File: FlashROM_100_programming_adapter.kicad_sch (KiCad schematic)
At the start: 2 parts

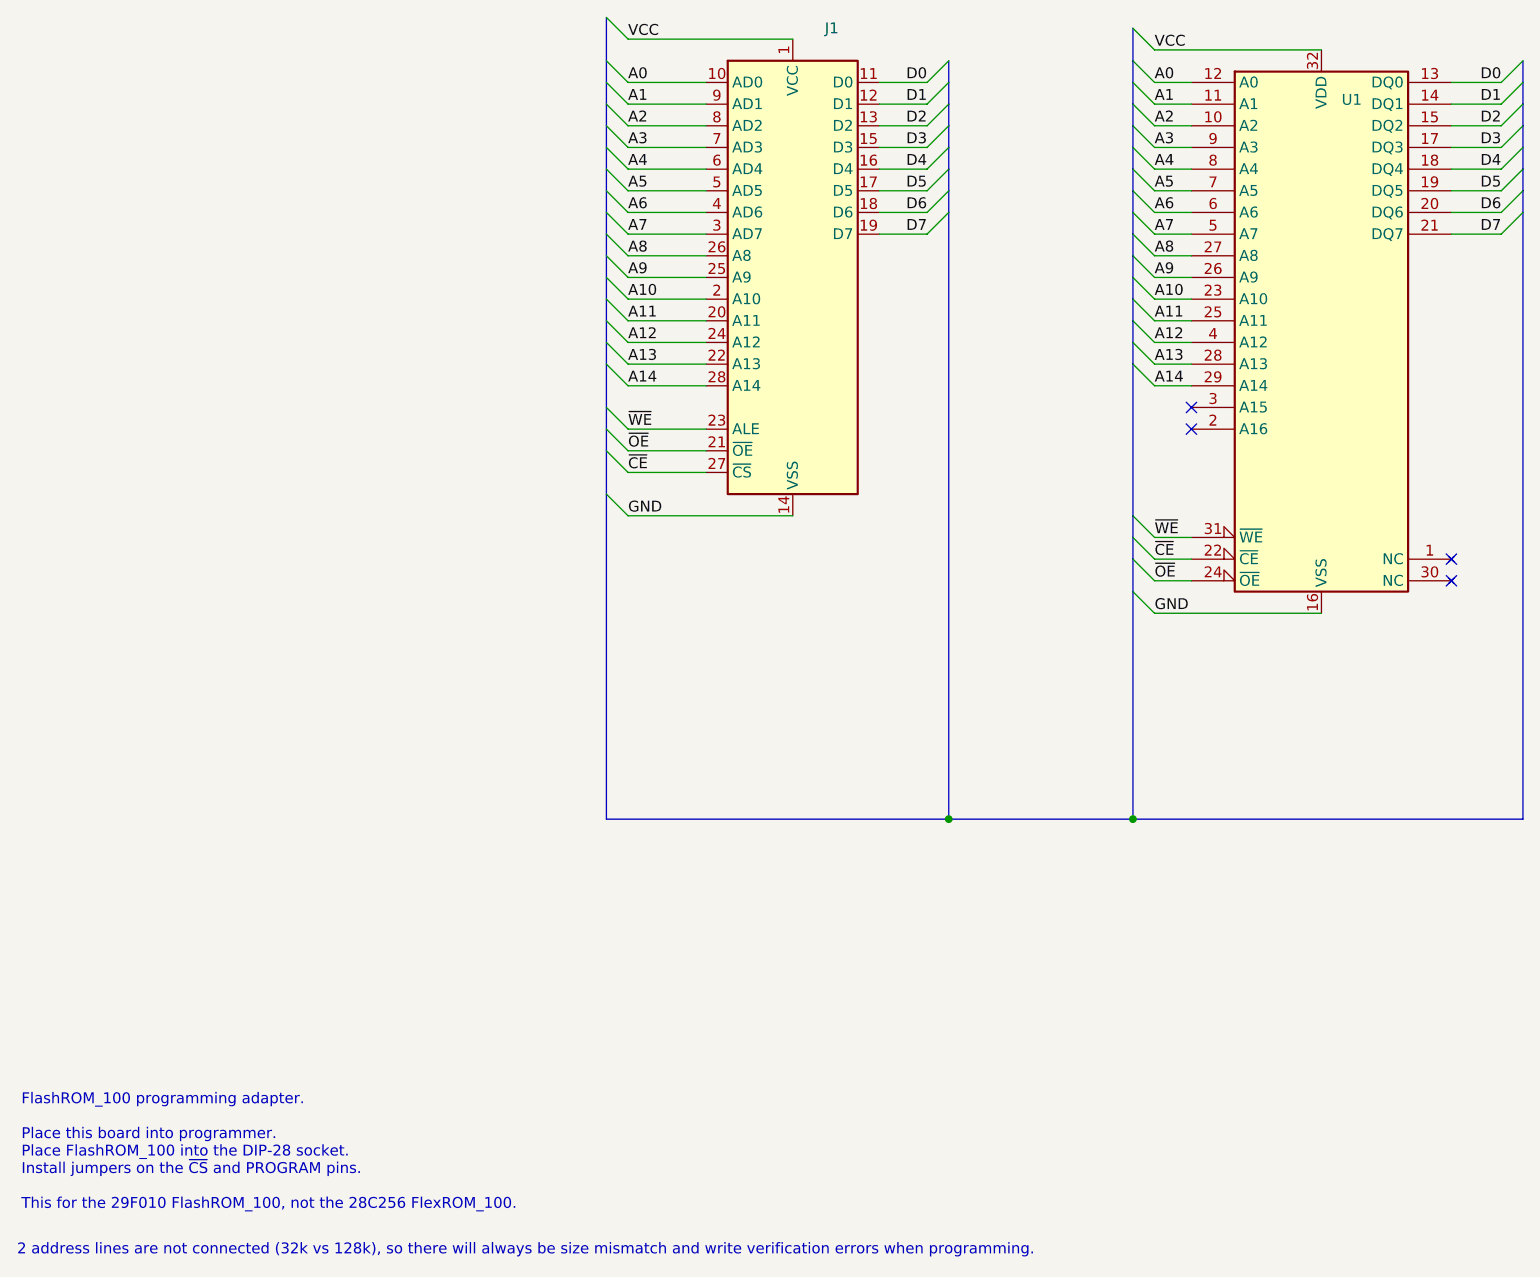
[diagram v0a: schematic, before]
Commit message: Fix wrong pinout on FlashROM_100 TSOPgit add -A!
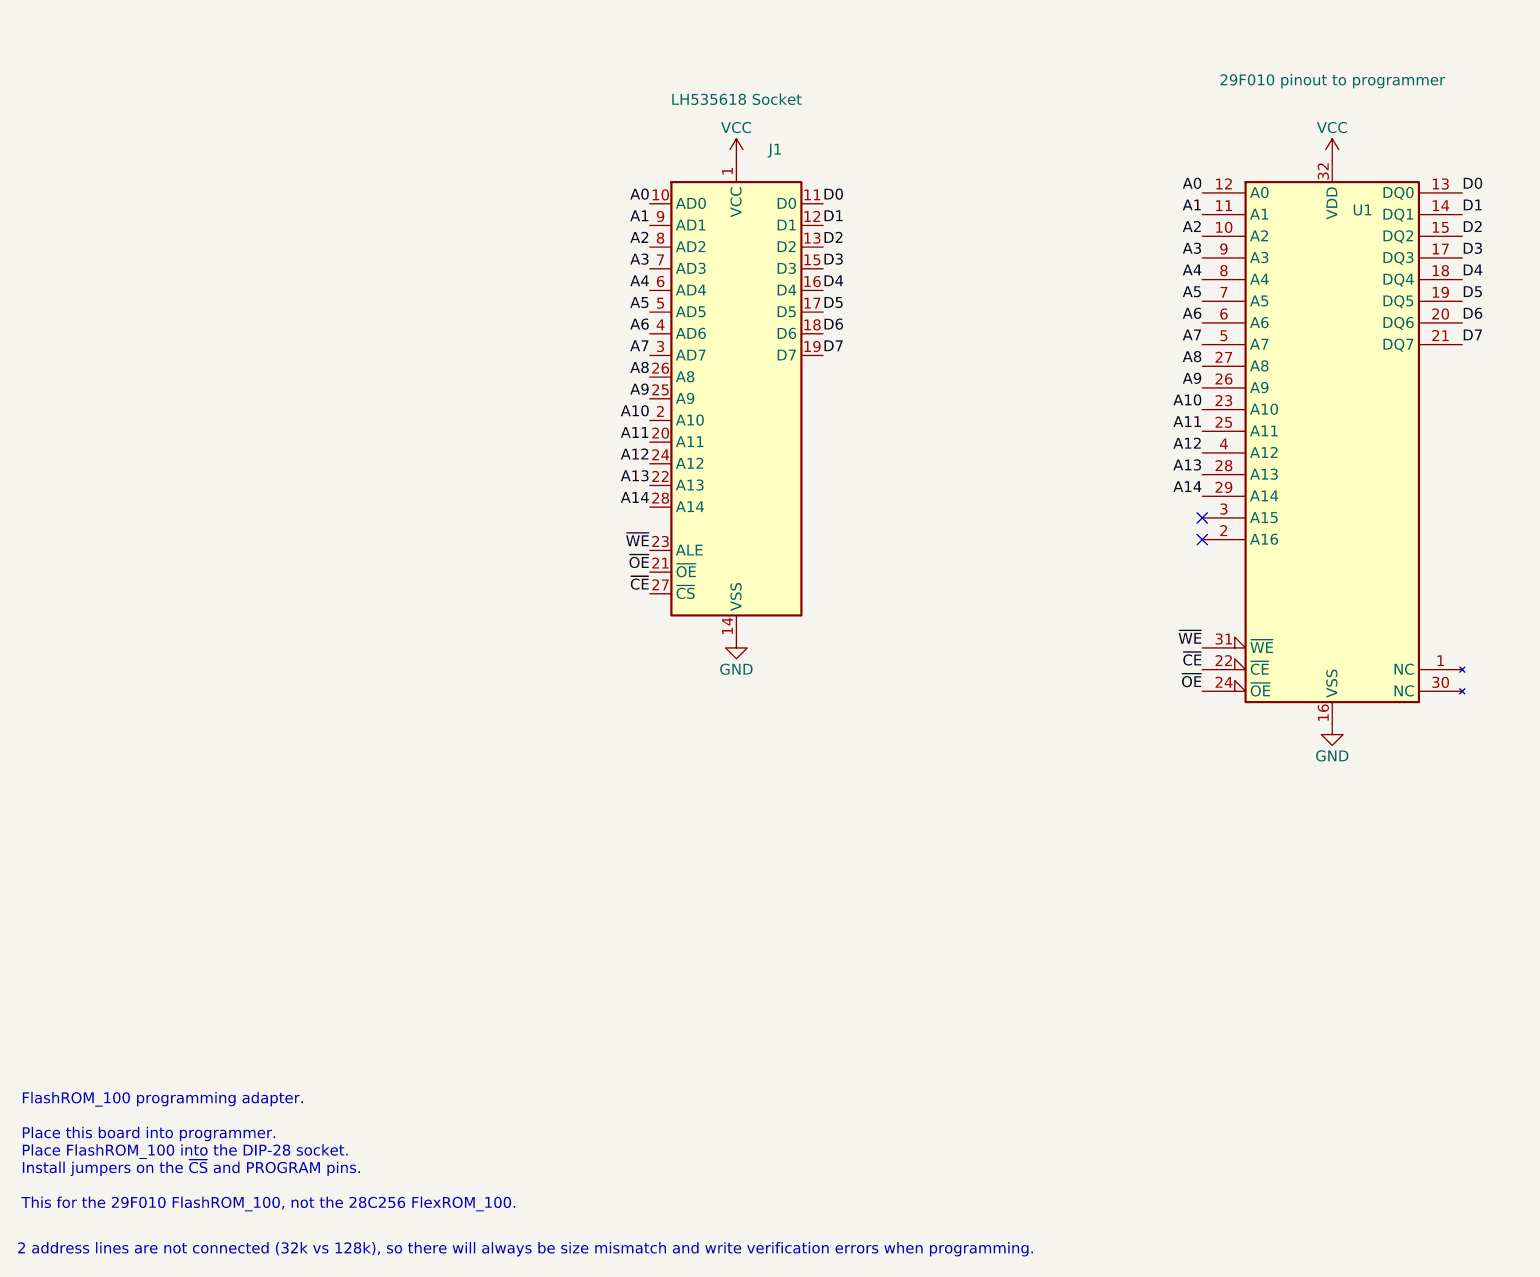
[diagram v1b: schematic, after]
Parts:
- J1: value (none) -> LH535618 Socket; footprint (none) -> 000_LOCAL:DIP28_0.6
- U1: value (none) -> 29F010 pinout to programmer; footprint (none) -> 000_LOCAL:DIP32_0.3
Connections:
- no-connect marks 4 -> 2
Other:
- moved on the sheet: J1, U1
